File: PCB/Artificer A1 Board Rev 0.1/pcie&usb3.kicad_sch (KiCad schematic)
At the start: 23 parts, among them J2 Conn_01x02, U16 HD3SS3202IRSVR, U17 X3113WVS-36-9TV01, U18 HC-USB3.0-L168-WP

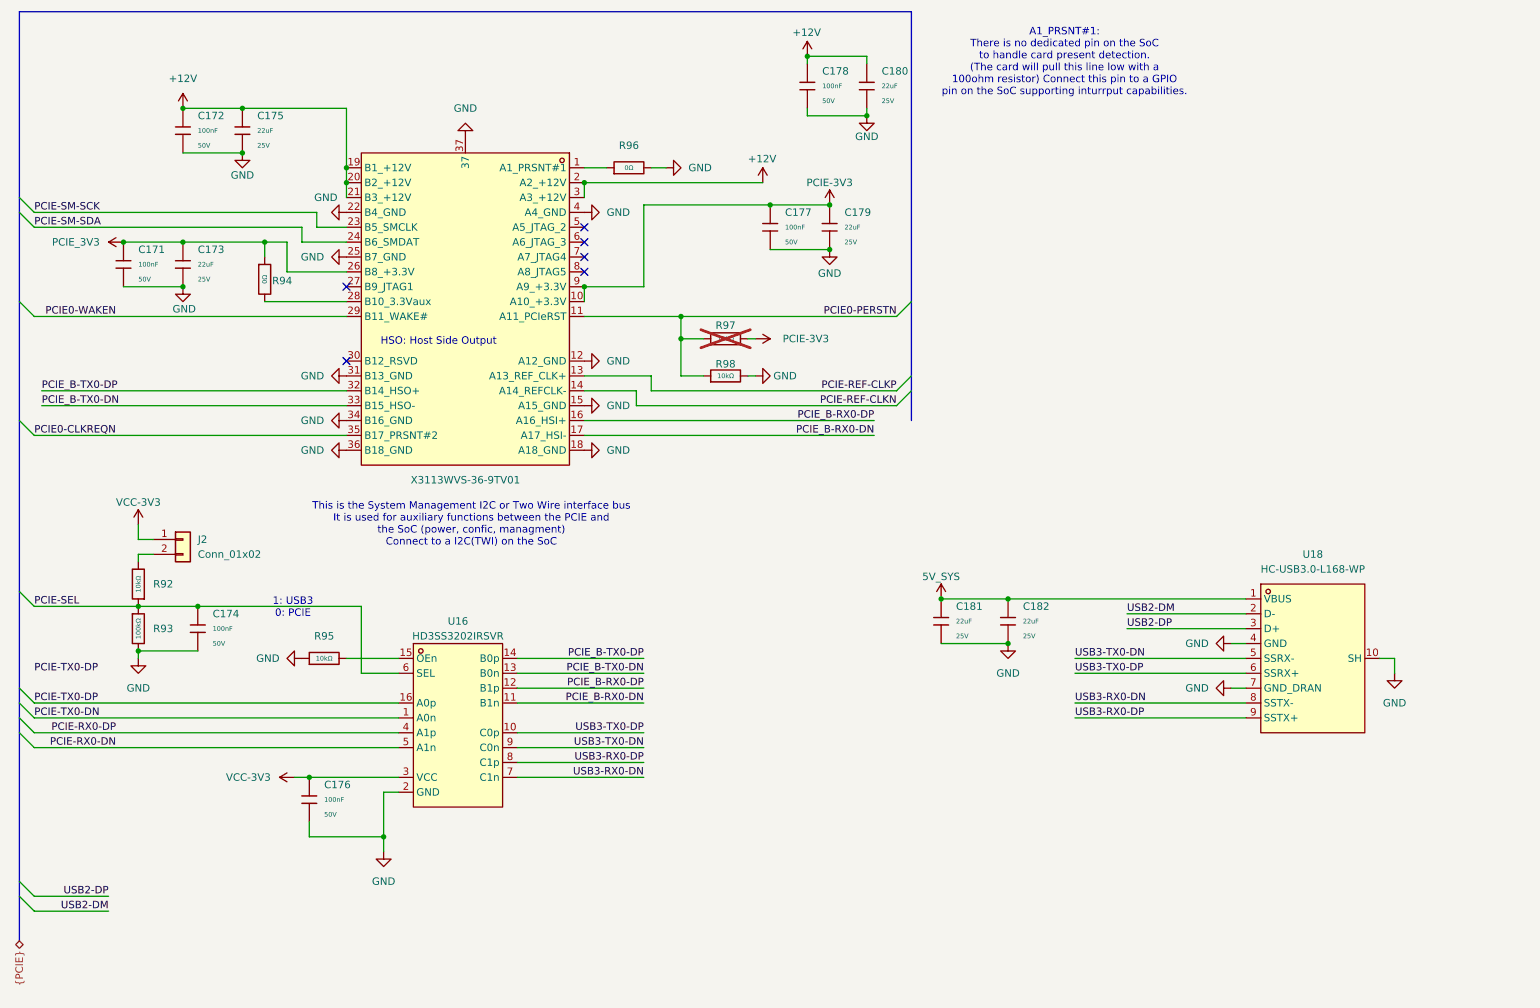
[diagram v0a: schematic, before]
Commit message: placed all components
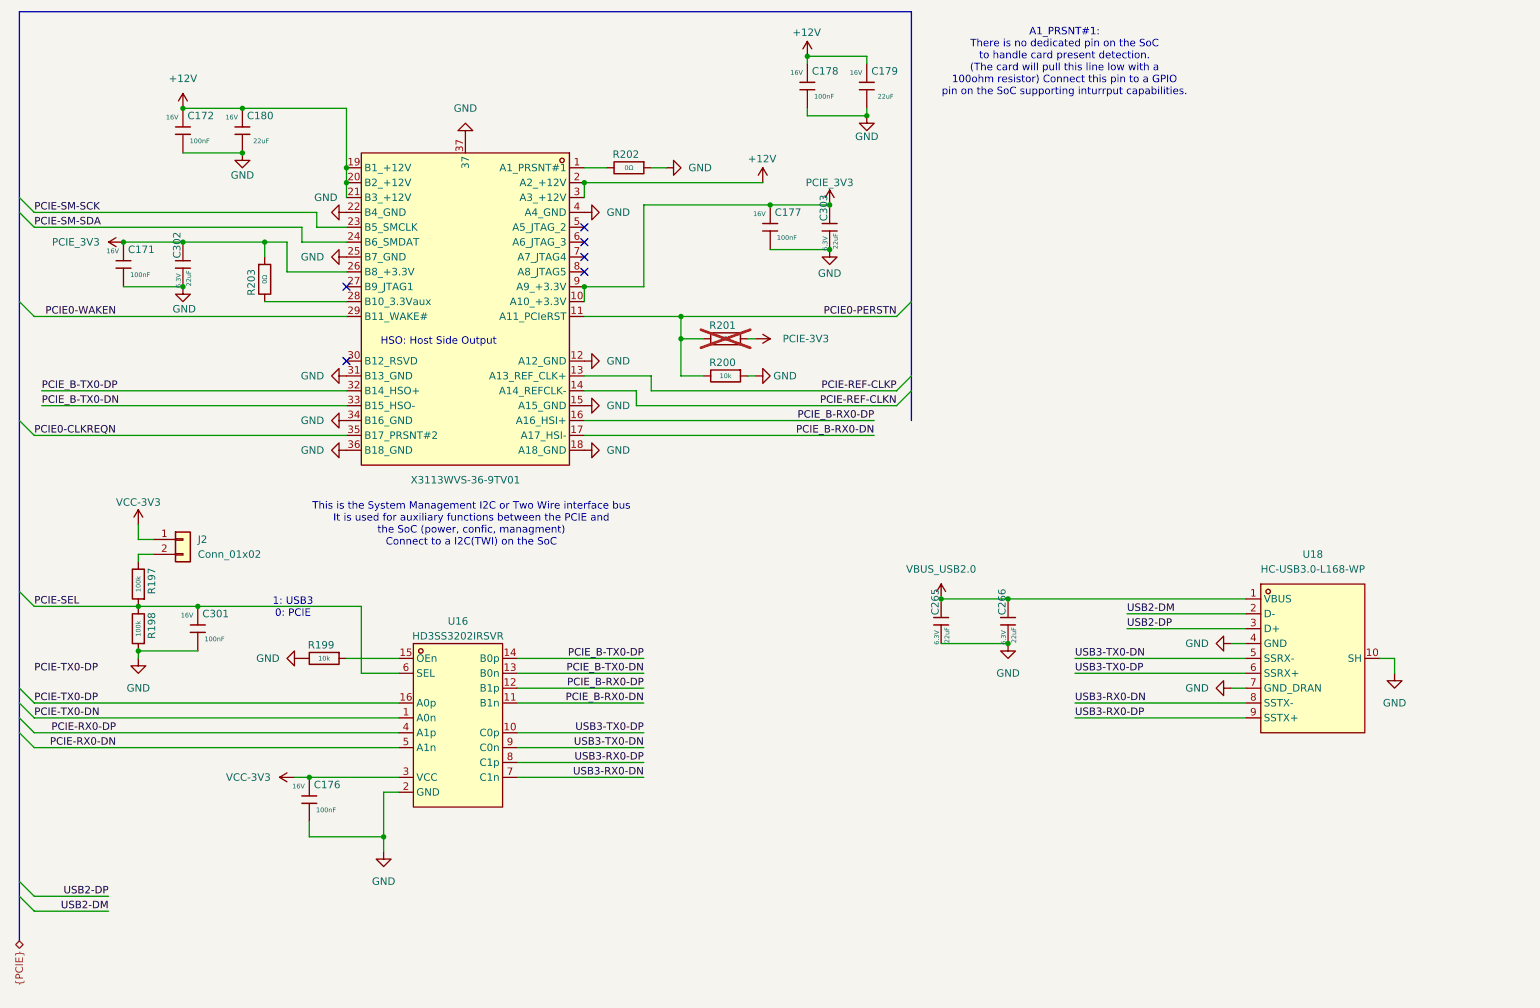
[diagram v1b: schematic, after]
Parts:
- removed C171, C172, C174, C176, C177, C178: 100nF, PCM_JLCPCB:C_0402, symbol PCM_JLCPCB-Capacitors:0402,100nF,(2)
- removed C173, C175, C179, C180, C181, C182: 22uF, PCM_JLCPCB:C_0805, symbol PCM_JLCPCB-Capacitors:0805,22uF
- removed R92, R95, R97, R98: 10kΩ, PCM_JLCPCB:R_0402, symbol PCM_JLCPCB-Resistors:0402,10kΩ
- removed R93: 100kΩ, PCM_JLCPCB:R_0402, symbol PCM_JLCPCB-Resistors:0402,100kΩ
- removed R94, R96: 0Ω, PCM_JLCPCB:R_0402, symbol PCM_JLCPCB-Resistors:0402,0Ω
- added C171, C172, C176, C177, C178, C301: 100nF, Capacitor_SMD:C_0201_0603Metric, symbol Cap:JLCPCB_Lib_Blank_Cap
- added C179, C180, C265, C266, C302, C303: 22uF, Capacitor_SMD:C_0603_1608Metric, symbol Cap:JLCPCB_Lib_Blank_Cap
- added R197, R198: 100k, Resistor_SMD:R_0201_0603Metric, symbol Cap:JLCPCB_Res_Custom
- added R199: 10k, Resistor_SMD:R_0201_0603Metric, symbol Cap:JLCPCB_Res_Custom
- added R200, R201: 10k, Resistor_SMD:R_0402_1005Metric, symbol Cap:JLCPCB_Res_Custom
- added R202, R203: 0Ω, Resistor_SMD:R_0402_1005Metric, symbol Cap:JLCPCB_Res_Custom
- J2: footprint Connector_PinHeader_2.54mm:PinHeader_1x02_P2.54mm_Vertical -> Connector_PinHeader_1.27mm:PinHeader_1x02_P1.27mm_Vertical
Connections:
- net +12V: now also C172.2, C178.2, C179.2, C180.2
- net GND: now also C171.1, C172.1, C176.1, C177.1, C178.1, C179.1, C180.1, C265.1, C266.1, C301.1, C302.1, C303.1, R198.1, R199.2, R200.1, R202.1
- net PCIE-3V3: now also R201.1; no longer U17.10 (A10_+3.3V), U17.9 (A9_+3.3V)
- net PCIE-SEL: now also C301.2, R197.1, R198.2
- net PCIE0-PERSTN: now also R200.2, R201.2
- net PCIE_3V3: now also U17.10 (A10_+3.3V), U17.9 (A9_+3.3V), C171.2, C177.2, C302.2, C303.2, R203.1
- net VCC-3V3: now also C176.2
- net at J2.2 (Pin_2): now also R197.2
- net at U16.15 (OEn): now also R199.1
- net at U17.1 (A1_PRSNT#1): now also R202.2
- net at U17.28 (B10_3.3Vaux): now also R203.2
- net 5V_SYS renamed VBUS_USB2.0
- net VBUS_USB2.0: now also C265.2, C266.2
- net PCIE-REF-CLKN  renamed PCIE-REF-CLKN
- net PCIE-REF-CLKP  renamed PCIE-REF-CLKP

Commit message: started routing
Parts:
- removed U18: HC-USB3.0-L168-WP, easyeda:USB-TH_USB3.0-A, symbol easyeda:HC-USB3.0-L168-WP
- added U7: X1618WVS-36-9TV15, easyeda:CONN-SMD-X1618WVS-36-9TV15, symbol easyeda:X1618WVS-36-9TV15
- added USB4: HC-USB3.0-L168-WJ, easyeda:USB-3.0-A-TH_HC-USB3.0-L168-WJ, symbol easyeda:HC-USB3.0-L168-WJ
- J2: footprint Connector_PinHeader_1.27mm:PinHeader_1x02_P1.27mm_Vertical -> Connector_PinHeader_2.54mm:PinHeader_1x02_P2.54mm_Vertical
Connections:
- net GND: now also USB4.10 (GND), USB4.11 (GND), USB4.4 (GND), USB4.7 (GND_DRAIN)
- net PCIE-RX0-DN: now also U16.4 (A1p); no longer U16.5 (A1n)
- net PCIE-RX0-DP: now also U16.5 (A1n); no longer U16.4 (A1p)
- net PCIE-TX0-DN: now also U16.16 (A0p); no longer U16.1 (A0n)
- net PCIE-TX0-DP: now also U16.1 (A0n); no longer U16.16 (A0p)
- net PCIE_B-RX0-DN: now also U16.12 (B1p); no longer U16.11 (B1n)
- net PCIE_B-RX0-DP: now also U16.11 (B1n); no longer U16.12 (B1p)
- net PCIE_B-TX0-DN: now also U16.14 (B0p); no longer U16.13 (B0n)
- net PCIE_B-TX0-DP: now also U16.13 (B0n); no longer U16.14 (B0p)
- net USB2-DP: now also USB4.3 (D+)
- net USB3-RX0-DN: now also U16.8 (C1p), USB4.8 (STDA_SSTX-); no longer U16.7 (C1n)
- net USB3-RX0-DP: now also U16.7 (C1n), USB4.9 (STDA_SSTX+); no longer U16.8 (C1p)
- net USB3-TX0-DN: now also U16.10 (C0p), USB4.5 (STDA_SSRX-); no longer U16.9 (C0n)
- net USB3-TX0-DP: now also U16.9 (C0n), USB4.6 (STDA_SSRX+); no longer U16.10 (C0p)
- net VBUS_USB2.0: now also USB4.1 (VBUS)
- new net USB2-DN: USB4.2 (D-)
- no-connect marks 6 -> 8

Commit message: finsihed more routing
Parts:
- R197: value 100k -> 1k
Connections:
- net PCIE0-WAKEN  renamed PCIE0-WAKEN
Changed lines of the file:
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@@
 	)
 	(bus_entry
-		(at 177.8 81.28)
-		(size -2.54 2.54)
+		(at 25.4 68.58)
+		(size 2.54 2.54)
 		(stroke
 			(width 0)
@@
 	)
 	(bus_entry
-		(at 25.4 137.16)
-		(size 2.54 2.54)
+		(at 177.8 81.28)
+		(size -2.54 2.54)
 		(stroke
 			(width 0)
@@
 	)
 	(bus_entry
-		(at 25.4 68.58)
+		(at 25.4 137.16)
 		(size 2.54 2.54)
 		(stroke
@@
 	(bus
 		(pts
-			(xy 25.4 53.34) (xy 25.4 68.58)
-		)
-		(stroke
-			(width 0)
-			(type default)
-		)
-	)
-	(bus
-		(pts
 			(xy 25.4 137.16) (xy 25.4 139.7)
 		)
@@
 	(bus
 		(pts
-			(xy 177.8 68.58) (xy 177.8 88.9)
+			(xy 177.8 19.05) (xy 177.8 88.9)
 		)
 		(stroke
@@
 		)
 	)
-	(bus
-		(pts
-			(xy 177.8 19.05) (xy 177.8 68.58)
-		)
-		(stroke
-			(width 0)
-			(type default)
-		)
-	)
 	(wire
 		(pts
@@
 	(bus
 		(pts
-			(xy 25.4 68.58) (xy 25.4 88.9)
+			(xy 25.4 53.34) (xy 25.4 88.9)
 		)
 		(stroke
@@
 		)
 	)
-	(label "PCIE0-WAKEN "
-		(at 41.91 71.12 180)
+	(label "PCIE0-WAKEN"
+		(at 27.94 71.12 0)
+		(effects
+			(font
+				(size 1.27 1.27)
+			)
+			(justify left bottom)
+		)
+	)
+	(label "PCIE0-PERSTN"
+		(at 175.26 71.12 180)
 		(effects
 			(font
@@
 		)
 	)
-	(label "PCIE0-PERSTN"
-		(at 175.26 71.12 180)
-		(effects
-			(font
-				(size 1.27 1.27)
-			)
-			(justify right bottom)
-		)
-	)
 	(label "PCIE_B-RX0-DN"
 		(at 132.08 134.62 180)
@@
 			)
 		)
-		(property "Value" "100k"
+		(property "Value" "1k"
 			(at 45.72 116.84 90)
 			(show_name no)

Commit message: more routing and decoupling
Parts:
- R202: value 0Ω -> 10k; footprint Resistor_SMD:R_0402_1005Metric -> Resistor_SMD:R_0201_0603Metric
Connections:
- net GND: no longer R202.1
- net VCC-3V3: now also R202.1
- net PCIE-CARD-PRESENT: now reaches R202.2, U17.1 (A1_PRSNT#1)
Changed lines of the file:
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@@
 	)
 	(junction
+		(at 125.73 45.72)
+		(diameter 0)
+		(color 0 0 0 0)
+	)
+	(junction
 		(at 170.18 36.83)
 		(diameter 0)
@@
 	)
 	(junction
-		(at 160.02 26.67)
+		(at 121.92 48.26)
 		(diameter 0)
 		(color 0 0 0 0)
 	)
 	(junction
-		(at 121.92 48.26)
+		(at 160.02 26.67)
 		(diameter 0)
 		(color 0 0 0 0)
@@
 	)
 	(bus_entry
+		(at 177.8 48.26)
+		(size -2.54 -2.54)
+		(stroke
+			(width 0)
+			(type default)
+		)
+	)
+	(bus_entry
 		(at 25.4 118.11)
 		(size 2.54 2.54)
@@
 	(wire
 		(pts
-			(xy 121.92 48.26) (xy 152.4 48.26)
+			(xy 121.92 48.26) (xy 140.97 48.26)
 		)
 		(stroke
@@
 	(wire
 		(pts
-			(xy 133.35 45.72) (xy 135.89 45.72)
+			(xy 125.73 43.18) (xy 125.73 45.72)
 		)
 		(stroke
@@
 	(wire
 		(pts
+			(xy 125.73 45.72) (xy 175.26 45.72)
+		)
+		(stroke
+			(width 0)
+			(type default)
+		)
+	)
+	(wire
+		(pts
 			(xy 214.63 121.92) (xy 234.95 121.92)
 		)
@@
 		)
 	)
+	(label "PCIE-CARD-PRESENT"
+		(at 175.26 45.72 180)
+		(effects
+			(font
+				(size 1.27 1.27)
+			)
+			(justify right bottom)
+		)
+	)
 	(hierarchical_label "{PCIE}"
 		(shape bidirectional)
@@
 	)
 	(symbol
-		(lib_id "Cap:JLCPCB_Res_Custom")
-		(at 129.54 45.72 270)
-		(unit 1)
-		(body_style 1)
-		(exclude_from_sim no)
-		(in_bom yes)
-		(on_board yes)
-		(in_pos_files yes)
-		(dnp no)
-		(property "Reference" "R202"
-			(at 126.746 43.434 90)
-			(show_name no)
-			(do_not_autoplace no)
-			(effects
-				(font
-					(size 1.27 1.27)
-				)
-				(justify left)
-			)
-		)
-		(property "Value" "0Ω"
-			(at 129.54 45.72 90)
-			(show_name no)
-			(do_not_autoplace yes)
-			(effects
-				(font
-					(size 0.8 0.8)
-				)
-			)
-		)
-		(property "Footprint" "Resistor_SMD:R_0402_1005Metric"
-			(at 129.54 43.942 90)
-			(hide yes)
-			(show_name no)
-			(do_not_autoplace no)
-			(effects
-				(font
-					(size 1.27 1.27)
-				)
-			)
-		)
-		(property "Datasheet" ""
-			(at 129.54 45.72 0)
-			(hide yes)
-			(show_name no)
-			(do_not_autoplace no)
-			(effects
-				(font
-					(size 1.27 1.27)
-				)
-			)
-		)
-		(property "Description" ""
-			(at 129.54 45.72 0)
-			(hide yes)
-			(show_name no)
-			(do_not_autoplace no)
-			(effects
-				(font
-					(size 1.27 1.27)
-				)
-			)
-		)
-		(pin "1"
-		)
-		(pin "2"
-		)
-		(instances
-			(project "Artificer A1 Board Rev 0.1"
-				(path "/7c37bdb5-94b0-4567-b5ec-a879db855389/fc53f3ee-65f7-486b-9f15-3d3dc12df657"
-					(reference "R202")
-					(unit 1)
-				)
-			)
-		)
-	)
-	(symbol
 		(lib_id "power:GND")
 		(at 53.34 66.04 0)
@@
 	)
 	(symbol
-		(lib_id "power:GND")
-		(at 135.89 45.72 90)
-		(unit 1)
-		(body_style 1)
-		(exclude_from_sim no)
-		(in_bom yes)
-		(on_board yes)
-		(in_pos_files yes)
-		(dnp no)
-		(fields_autoplaced yes)
-		(property "Reference" "#PWR0378"
-			(at 142.24 45.72 0)
-			(hide yes)
-			(show_name no)
-			(do_not_autoplace no)
-			(effects
-				(font
-					(size 1.27 1.27)
-				)
-			)
-		)
-		(property "Value" "GND"
-			(at 139.7 45.7199 90)
-			(show_name no)
-			(do_not_autoplace no)
-			(effects
-				(font
-					(size 1.27 1.27)
-				)
-				(justify right)
-			)
-		)
-		(property "Footprint" ""
-			(at 135.89 45.72 0)
-			(hide yes)
-			(show_name no)
-			(do_not_autoplace no)
-			(effects
-				(font
-					(size 1.27 1.27)
-				)
-			)
-		)
-		(property "Datasheet" ""
-			(at 135.89 45.72 0)
-			(hide yes)
-			(show_name no)
-			(do_not_autoplace no)
-			(effects
-				(font
-					(size 1.27 1.27)
-				)
-			)
-		)
-		(property "Description" "Power symbol creates a global label with name \"GND\" , ground"
-			(at 135.89 45.72 0)
-			(hide yes)
-			(show_name no)
-			(do_not_autoplace no)
-			(effects
-				(font
-					(size 1.27 1.27)
-				)
-			)
-		)
-		(pin "1"
-		)
-		(instances
-			(project "Artificer A1 Board Rev 0.1"
-				(path "/7c37bdb5-94b0-4567-b5ec-a879db855389/fc53f3ee-65f7-486b-9f15-3d3dc12df657"
-					(reference "#PWR0378")
-					(unit 1)
-				)
-			)
-		)
-	)
-	(symbol
 		(lib_id "Cap:JLCPCB_Lib_Blank_Cap")
 		(at 53.34 39.37 180)
@@
 	(symbol
 		(lib_id "power:+12V")
-		(at 152.4 48.26 0)
-		(mirror y)
+		(at 140.97 48.26 270)
+		(mirror x)
 		(unit 1)
 		(body_style 1)
@@
 		(dnp no)
 		(property "Reference" "#PWR0381"
-			(at 152.4 52.07 0)
+			(at 137.16 48.26 0)
 			(hide yes)
 			(show_name no)
@@
 		)
 		(property "Value" "+12V"
-			(at 149.86 44.196 0)
+			(at 149.352 48.26 90)
 			(show_name no)
 			(do_not_autoplace no)
@@
 		)
 		(property "Footprint" ""
-			(at 152.4 48.26 0)
+			(at 140.97 48.26 0)
 			(hide yes)
 			(show_name no)
@@
 		)
 		(property "Datasheet" ""
-			(at 152.4 48.26 0)
+			(at 140.97 48.26 0)
 			(hide yes)
 			(show_name no)
@@
 		)
 		(property "Description" "Power symbol creates a global label with name \"+12V\""
-			(at 152.4 48.26 0)
+			(at 140.97 48.26 0)
 			(hide yes)
 			(show_name no)
@@
 	(symbol
 		(lib_id "power:+5V")
+		(at 125.73 35.56 0)
+		(mirror y)
+		(unit 1)
+		(body_style 1)
+		(exclude_from_sim no)
+		(in_bom yes)
+		(on_board yes)
+		(in_pos_files yes)
+		(dnp no)
+		(property "Reference" "#PWR0378"
+			(at 125.73 39.37 0)
+			(hide yes)
+			(show_name no)
+			(do_not_autoplace no)
+			(effects
+				(font
+					(size 1.27 1.27)
+				)
+			)
+		)
+		(property "Value" "VCC-3V3"
+			(at 125.73 31.496 0)
+			(show_name no)
+			(do_not_autoplace no)
+			(effects
+				(font
+					(size 1.27 1.27)
+				)
+			)
+		)
+		(property "Footprint" ""
+			(at 125.73 35.56 0)
+			(hide yes)
+			(show_name no)
+			(do_not_autoplace no)
+			(effects
+				(font
+					(size 1.27 1.27)
+				)
+			)
+		)
+		(property "Datasheet" ""
+			(at 125.73 35.56 0)
+			(hide yes)
+			(show_name no)
+			(do_not_autoplace no)
+			(effects
+				(font
+					(size 1.27 1.27)
+				)
+			)
+		)
+		(property "Description" "Power symbol creates a global label with name \"+5V\""
+			(at 125.73 35.56 0)
+			(hide yes)
+			(show_name no)
+			(do_not_autoplace no)
+			(effects
+				(font
+					(size 1.27 1.27)
+				)
+			)
+		)
+		(pin "1"
+		)
+		(instances
+			(project "Artificer A1 Board Rev 0.1"
+				(path "/7c37bdb5-94b0-4567-b5ec-a879db855389/fc53f3ee-65f7-486b-9f15-3d3dc12df657"
+					(reference "#PWR0378")
+					(unit 1)
+				)
+			)
+		)
+	)
+	(symbol
+		(lib_id "power:+5V")
 		(at 45.72 106.68 0)
 		(unit 1)
@@
 					(unit 1)
 				)
+			)
+		)
+	)
+	(symbol
+		(lib_id "Cap:JLCPCB_Res_Custom")
+		(at 125.73 39.37 0)
+		(unit 1)
+		(body_style 1)
+		(exclude_from_sim no)
+		(in_bom yes)
+		(on_board yes)
+		(in_pos_files yes)
+		(dnp no)
+		(property "Reference" "R202"
+			(at 123.444 42.164 90)
+			(show_name no)
+			(do_not_autoplace no)
+			(effects
+				(font
+					(size 1.27 1.27)
+				)
+				(justify left)
+			)
+		)
+		(property "Value" "10k"
+			(at 125.73 39.37 90)
+			(show_name no)
+			(do_not_autoplace yes)
+			(effects
+				(font
+					(size 0.8 0.8)
+				)
+			)
+		)
+		(property "Footprint" "Resistor_SMD:R_0201_0603Metric"
+			(at 123.952 39.37 90)
+			(hide yes)
+			(show_name no)
+			(do_not_autoplace no)
+			(effects
+				(font
+					(size 1.27 1.27)
+				)
+			)
+		)
+		(property "Datasheet" ""
+			(at 125.73 39.37 0)
+			(hide yes)
+			(show_name no)
+			(do_not_autoplace no)
+			(effects
+				(font
+					(size 1.27 1.27)
+				)
+			)
+		)
+		(property "Description" ""
+			(at 125.73 39.37 0)
+			(hide yes)
+			(show_name no)
+			(do_not_autoplace no)
+			(effects
+				(font
+					(size 1.27 1.27)
+				)
+			)
+		)
+		(pin "1"
+		)
+		(pin "2"
+		)
+		(instances
+			(project "Artificer A1 Board Rev 0.1"
+				(path "/7c37bdb5-94b0-4567-b5ec-a879db855389/fc53f3ee-65f7-486b-9f15-3d3dc12df657"
+					(reference "R202")
+					(unit 1)
+				)

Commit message: added power and gnd vias
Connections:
- net 3.3Vaux: now reaches R203.2, U17.28 (B10_3.3Vaux)
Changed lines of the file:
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@@
+		)
+	)
+	(label "3.3Vaux"
+		(at 71.12 68.58 0)
+		(effects
+			(font
+				(size 1.27 1.27)
+			)
+			(justify left bottom)
 		)
 	)
